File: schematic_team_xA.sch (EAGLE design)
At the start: 19 parts, among them U1 ATMEGA328P-AU, U2 MPU-6050

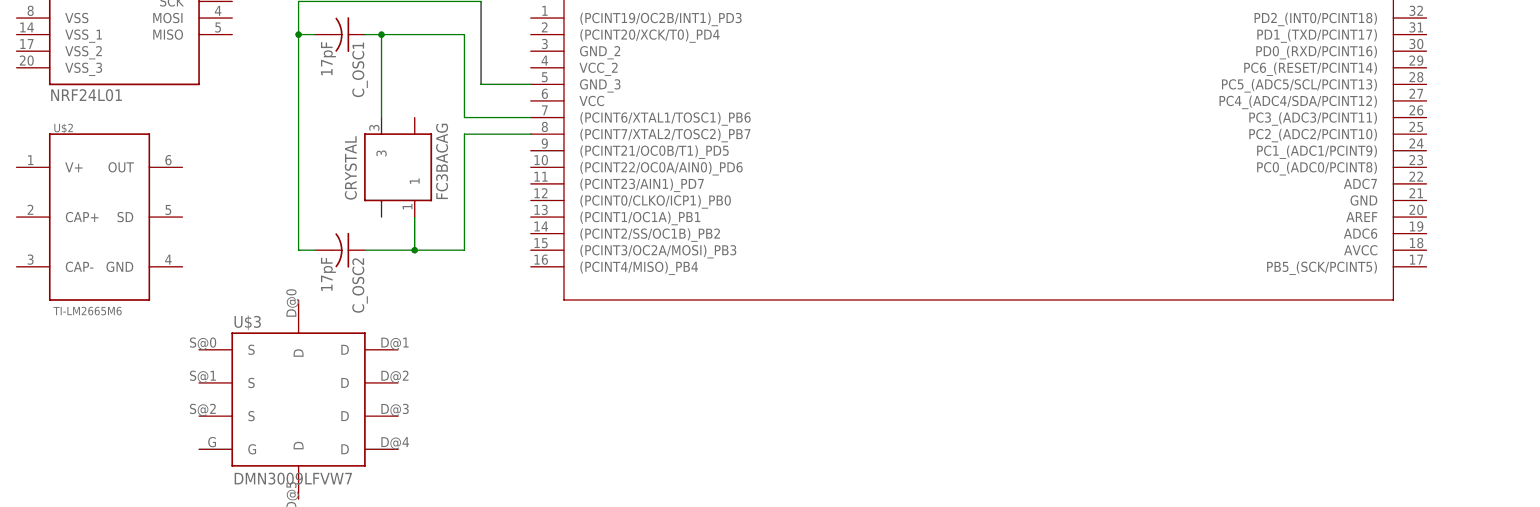
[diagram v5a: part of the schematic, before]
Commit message: Decoupler and charge pump
Added a decoupler to the AREF and adjusted the pad size on the charge pump
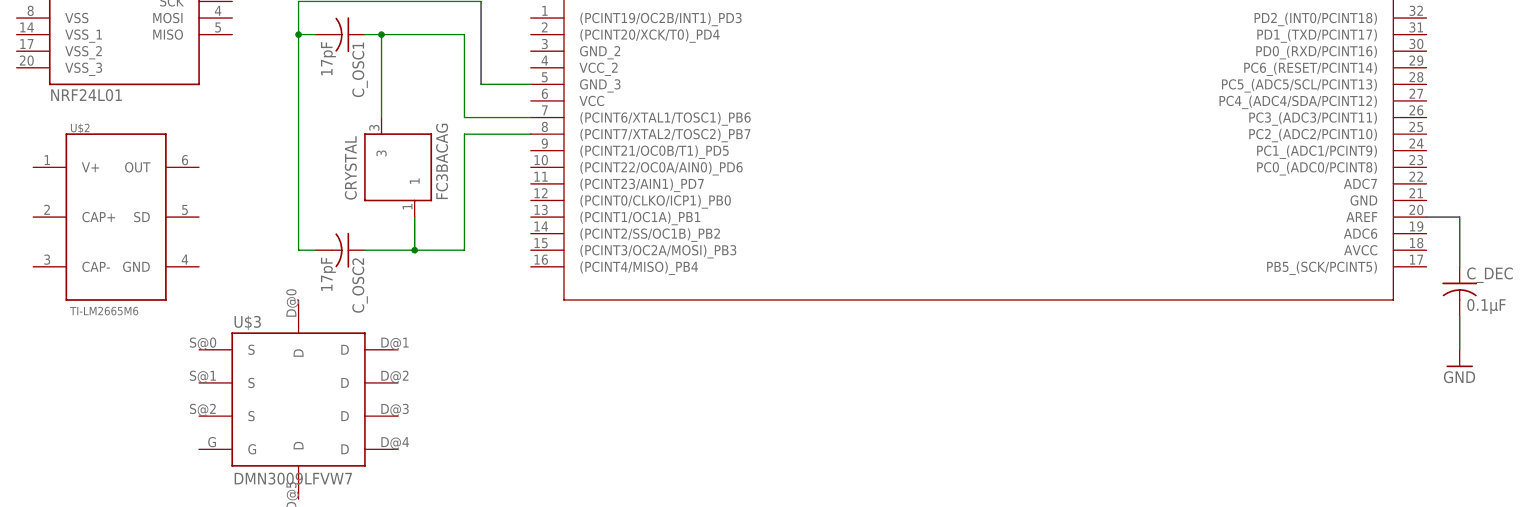
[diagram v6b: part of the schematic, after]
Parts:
- added C_DEC: 0.1μF, resistor:C-USC0805
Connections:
- new net GND: C_DEC.2
- new net N$4: C_DEC.1, U1.AREF
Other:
- moved on the sheet: U$2
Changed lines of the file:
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@@
 <part name="R_VD1" library="rcl" deviceset="R-US_" device="R0603" value="100kΩ"/>
 <part name="R_VD2" library="rcl" deviceset="R-US_" device="R0603" value="100kΩ"/>
-<part name="U$2" library="TI-LM2665M6" deviceset="TI-LM2665" device="M6"/>
 <part name="U2" library="MPU-6050" deviceset="MPU-6050" device=""/>
 <part name="U$3" library="DMN3009LFVW" deviceset="DMN3009LFVW" device="7"/>
@@
 <part name="C_OSC2" library="resistor" library_urn="urn:adsk.eagle:library:348" deviceset="C-US" device="C0805" package3d_urn="urn:adsk.eagle:package:26137/1" value="17pF"/>
 <part name="CRYSTAL" library="FC3BACAG" deviceset="FC3BACA" device="G"/>
+<part name="GND1" library="supply1" deviceset="GND" device=""/>
+<part name="C_DEC" library="resistor" library_urn="urn:adsk.eagle:library:348" deviceset="C-US" device="C0805" package3d_urn="urn:adsk.eagle:package:26137/1" value="0.1μF"/>
+<part name="U$2" library="TI-LM2665M6" deviceset="TI-LM2665" device="M6"/>
 </parts>
 <sheets>
@@
 <instance part="R_VD1" gate="G$1" x="53.34" y="81.28"/>
 <instance part="R_VD2" gate="G$1" x="53.34" y="73.66"/>
-<instance part="U$2" gate="G$1" x="-12.7" y="15.24"/>
 <instance part="U2" gate="G$1" x="132.08" y="78.74"/>
 <instance part="U$3" gate="G$1" x="17.78" y="-12.7"/>
@@
 <instance part="C_OSC2" gate="G$1" x="25.4" y="10.16" rot="R270"/>
 <instance part="CRYSTAL" gate="G$1" x="33.02" y="22.86" rot="R90"/>
+<instance part="GND1" gate="1" x="195.58" y="-7.62"/>
+<instance part="C_DEC" gate="G$1" x="195.58" y="5.08"/>
+<instance part="U$2" gate="G$1" x="-10.16" y="15.24"/>
 </instances>
 <busses>
@@
 <wire x1="43.18" y1="30.48" x2="43.18" y2="43.18" width="0.1524" layer="91"/>
 <wire x1="43.18" y1="43.18" x2="30.48" y2="43.18" width="0.1524" layer="91"/>
+<pinref part="C_OSC1" gate="G$1" pin="1"/>
+<pinref part="CRYSTAL" gate="G$1" pin="3"/>
+<wire x1="30.48" y1="43.18" x2="27.94" y2="43.18" width="0.1524" layer="91"/>
 <wire x1="30.48" y1="30.48" x2="30.48" y2="43.18" width="0.1524" layer="91"/>
-<pinref part="C_OSC1" gate="G$1" pin="1"/>
-<wire x1="30.48" y1="43.18" x2="27.94" y2="43.18" width="0.1524" layer="91"/>
 <junction x="30.48" y="43.18"/>
-<pinref part="CRYSTAL" gate="G$1" pin="3"/>
 </segment>
 </net>
@@
 <pinref part="C_OSC2" gate="G$1" pin="1"/>
 <wire x1="43.18" y1="10.16" x2="35.56" y2="10.16" width="0.1524" layer="91"/>
+<pinref part="CRYSTAL" gate="G$1" pin="1"/>
 <wire x1="35.56" y1="10.16" x2="27.94" y2="10.16" width="0.1524" layer="91"/>
 <wire x1="35.56" y1="15.24" x2="35.56" y2="10.16" width="0.1524" layer="91"/>
 <junction x="35.56" y="10.16"/>
-<pinref part="CRYSTAL" gate="G$1" pin="1"/>
 </segment>
 </net>
@@
 </segment>
 </net>
+<net name="N$4" class="0">
+<segment>
+<pinref part="U1" gate="A" pin="AREF"/>
+<pinref part="C_DEC" gate="G$1" pin="1"/>
+<wire x1="190.5" y1="15.24" x2="195.58" y2="15.24" width="0.1524" layer="91"/>
+<wire x1="195.58" y1="15.24" x2="195.58" y2="7.62" width="0.1524" layer="91"/>
+</segment>
+</net>
+<net name="GND" class="0">
+<segment>
+<pinref part="GND1" gate="1" pin="GND"/>
+<pinref part="C_DEC" gate="G$1" pin="2"/>
+<wire x1="195.58" y1="-5.08" x2="195.58" y2="0" width="0.1524" layer="91"/>
+</segment>
+</net>

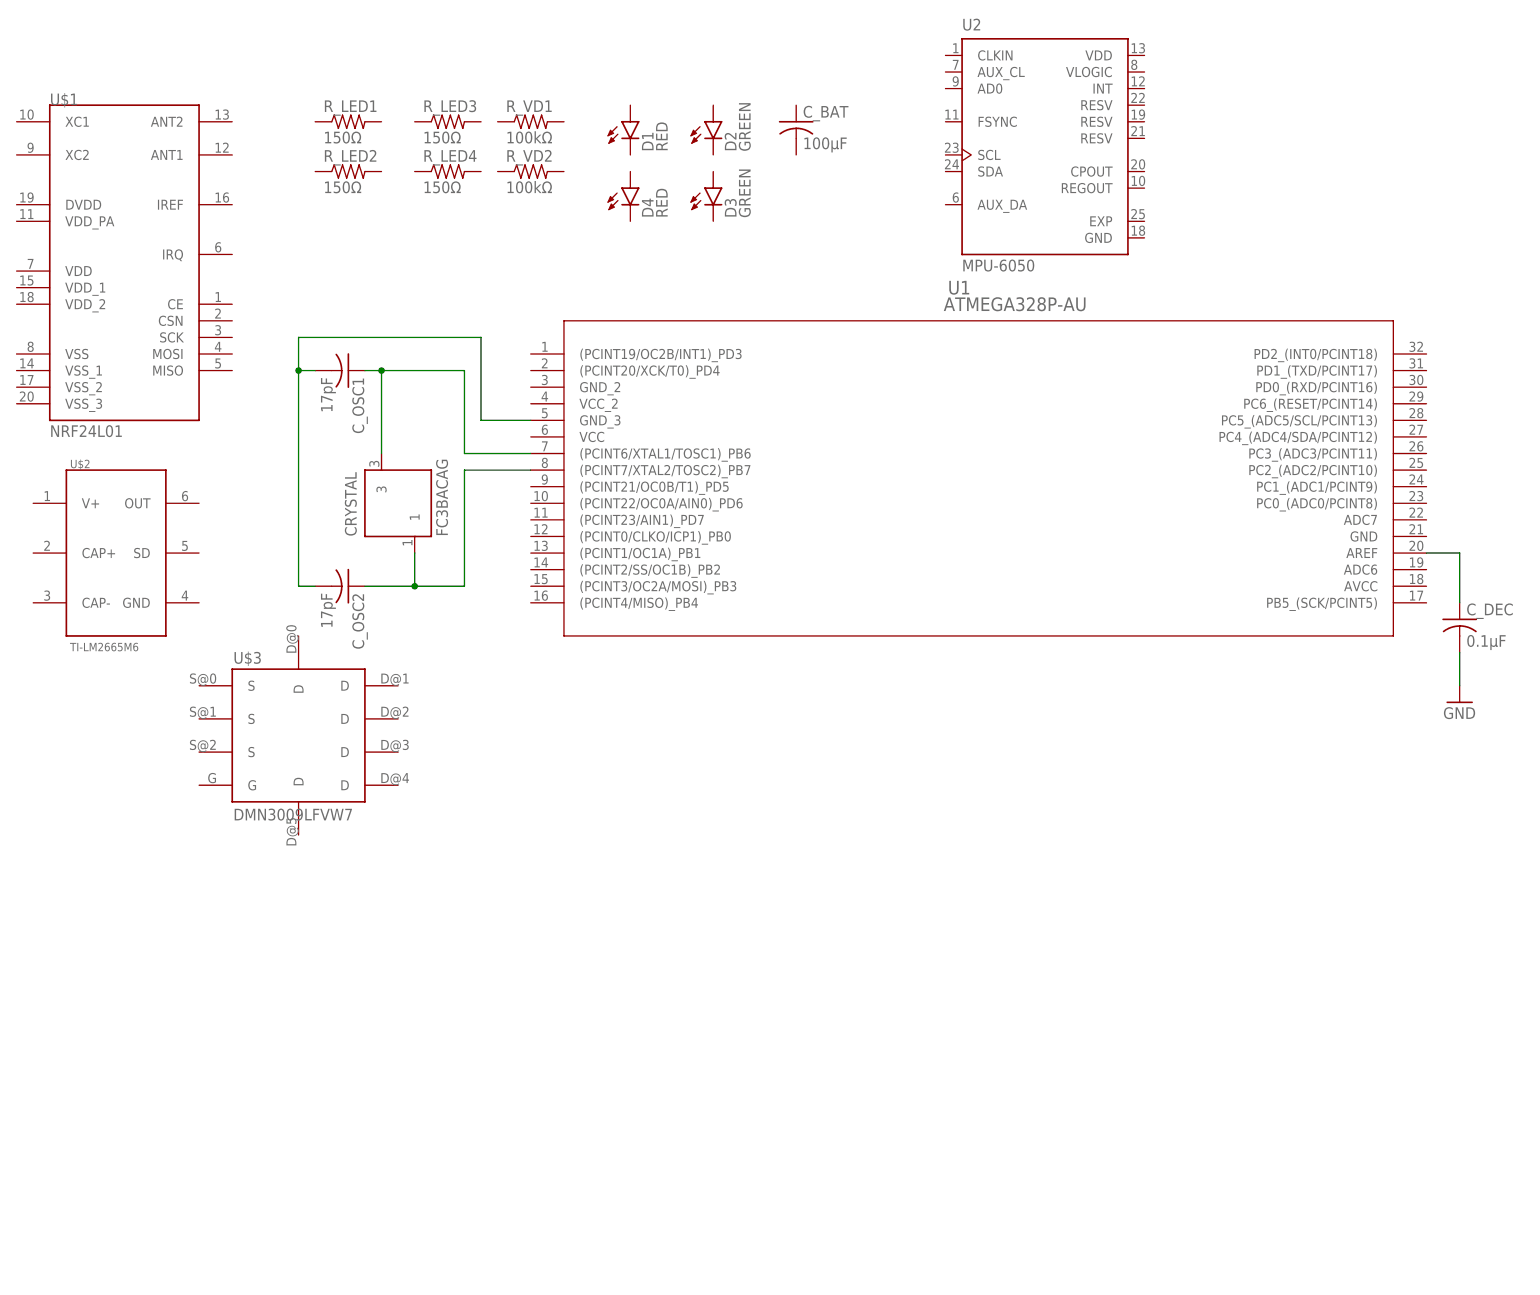
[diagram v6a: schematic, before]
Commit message: Basic Schematic
Schematic with Motor Low-side Driver and Crystal
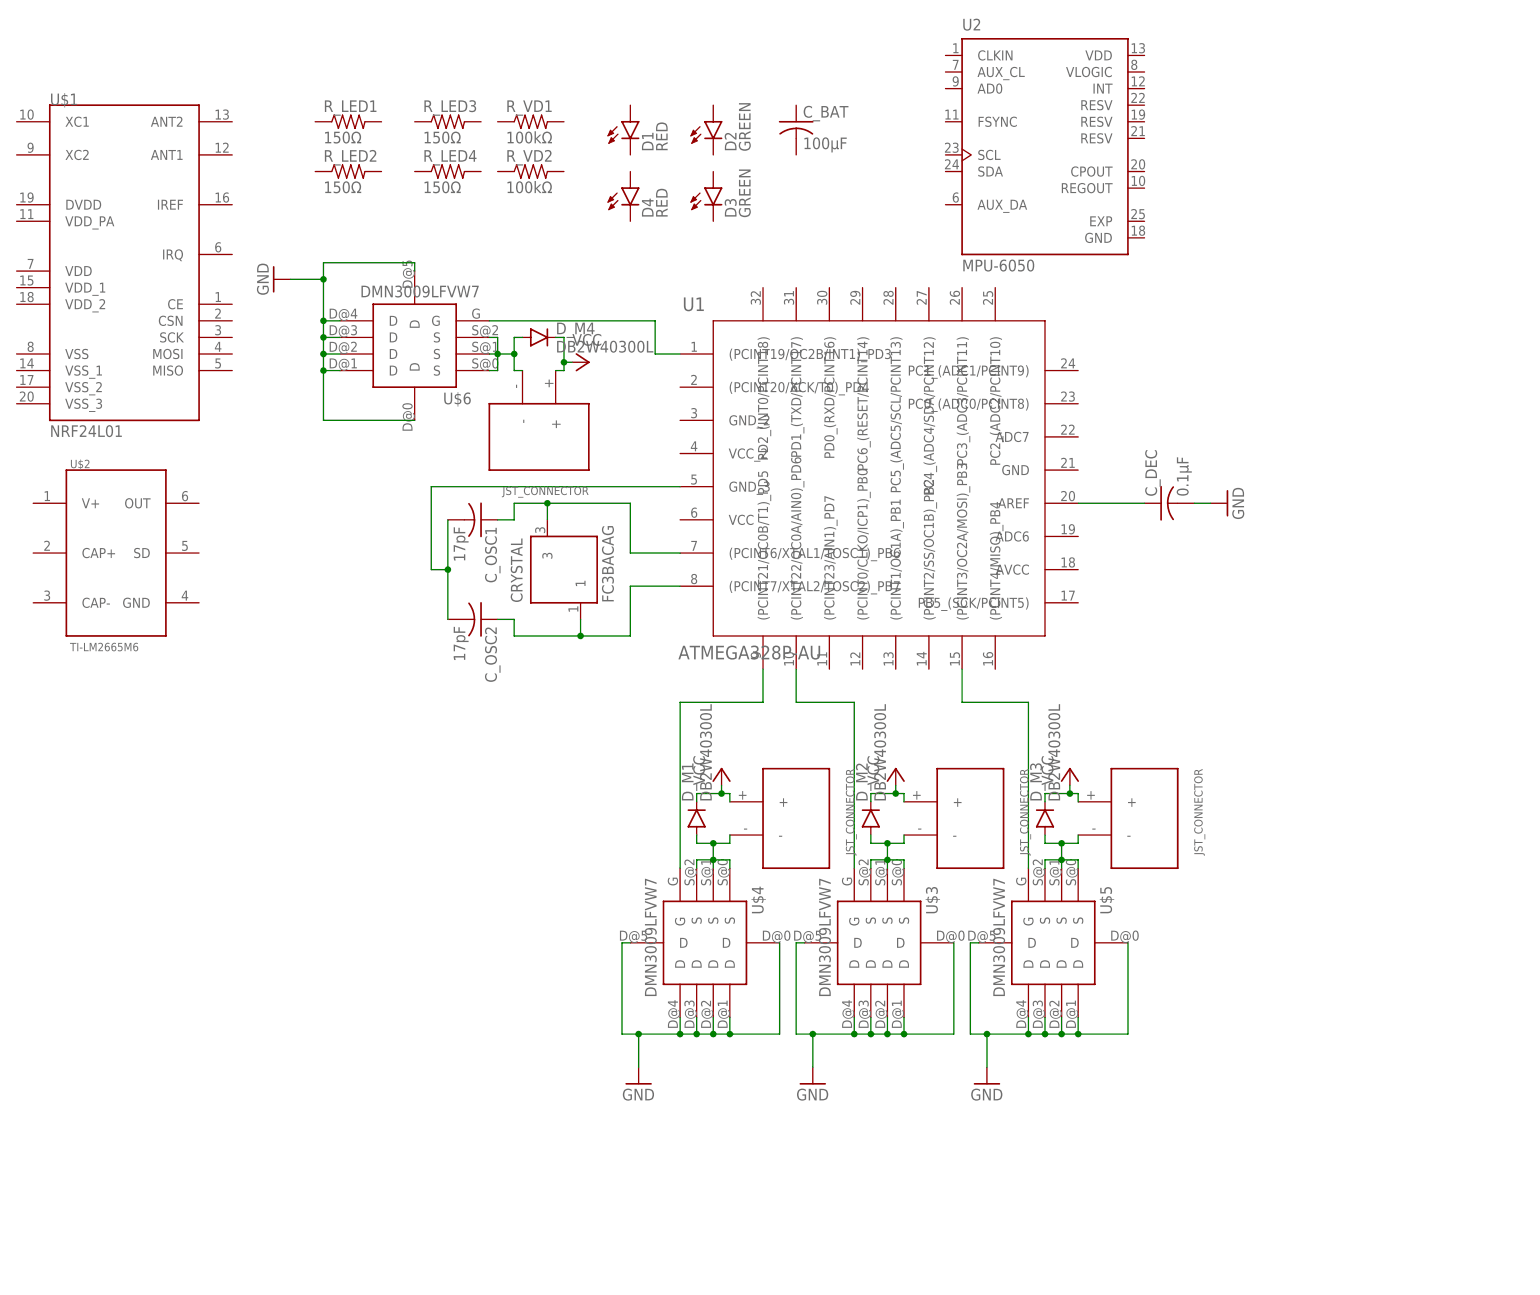
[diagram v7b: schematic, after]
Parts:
- added D_M1, D_M2, D_M3, D_M4: DB2W40300L, quad:DB2W40300L
- added MOTOR1, MOTOR2, MOTOR3, MOTOR4: JST_CONNECTOR_FEMALE, quad:JST_CONNECTOR_FEMALE
- added U$4, U$5, U$6: DMN3009LFVW7, DMN3009LFVW:DMN3009LFVW7
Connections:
- new net N$10: D_M1.PPIN, MOTOR1.-, U$4.S@0, U$4.S@1, U$4.S@2
- new net N$11: D_M3.PPIN, MOTOR3.-, U$5.S@0, U$5.S@1, U$5.S@2
- new net N$12: U$4.G, U1.(PCINT21/OC0B/T1)_PD5
- new net N$16: U$5.G, U1.(PCINT3/OC2A/MOSI)_PB3
- new net N$3: U$3.G, U1.(PCINT22/OC0A/AIN0)_PD6
- new net N$5: D_M4.PPIN, MOTOR4.-, U$6.S@0, U$6.S@1, U$6.S@2
- new net N$6: D_M2.PPIN, MOTOR2.-, U$3.S@0, U$3.S@1, U$3.S@2
- new net N$8: U$6.G, U1.(PCINT19/OC2B/INT1)_PD3
- new net VCC: D_M1.GPIN, D_M2.GPIN, D_M3.GPIN, D_M4.GPIN, MOTOR1.+, MOTOR2.+, MOTOR3.+, MOTOR4.+
- net GND: now also U$3.D@0, U$3.D@1, U$3.D@2, U$3.D@3, U$3.D@4, U$3.D@5, U$4.D@0, U$4.D@1, U$4.D@2, U$4.D@3, U$4.D@4, U$4.D@5, U$5.D@0, U$5.D@1, U$5.D@2, U$5.D@3, U$5.D@4, U$5.D@5, U$6.D@0, U$6.D@1, U$6.D@2, U$6.D@3, U$6.D@4, U$6.D@5
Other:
- moved on the sheet: CRYSTAL, C_DEC, C_OSC1, C_OSC2, U$3, U1

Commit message: Wired radio
Moved around motors to wire radio and connected the radio
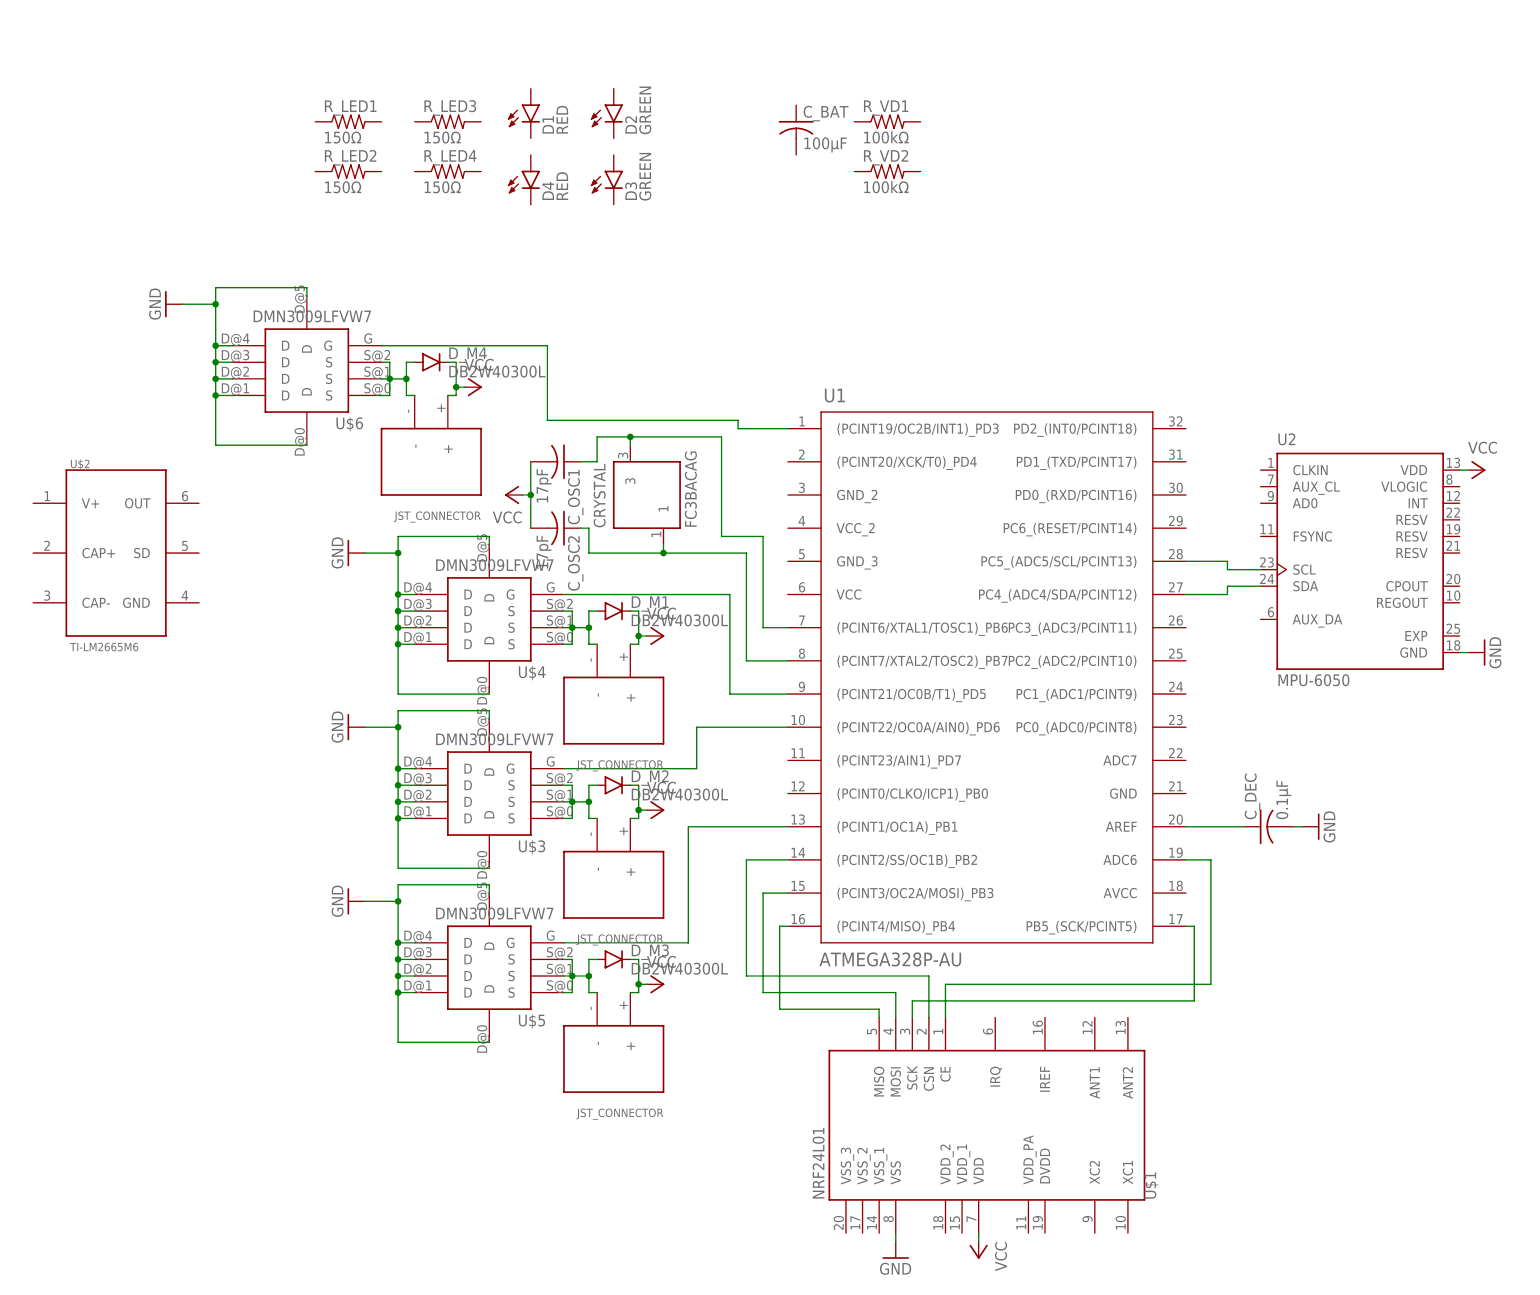
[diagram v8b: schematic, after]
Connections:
- new net N$1: U1.PC5_(ADC5/SCL/PCINT13), U2.SCL
- new net N$13: U$1.CE, U1.ADC6
- new net N$15: U$1.CSN, U1.(PCINT2/SS/OC1B)_PB2
- new net N$17: U$1.MOSI, U1.(PCINT3/OC2A/MOSI)_PB3
- new net N$18: U$1.MISO, U1.(PCINT4/MISO)_PB4
- new net N$19: U$1.SCK, U1.PB5_(SCK/PCINT5)
- net GND: now also U$1.VSS, U2.GND
- net N$16: now also U1.(PCINT1/OC1A)_PB1; no longer U1.(PCINT3/OC2A/MOSI)_PB3
- net N$7: now also U1.PC4_(ADC4/SDA/PCINT12), U2.SDA; no longer C_OSC1.2, C_OSC2.2, U1.GND_3
- net VCC: now also C_OSC1.2, C_OSC2.2, U$1.VDD, U2.VDD
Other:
- moved on the sheet: CRYSTAL, C_DEC, C_OSC1, C_OSC2, D1, D2, D3, D4, D_M1, D_M2, D_M3, D_M4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
